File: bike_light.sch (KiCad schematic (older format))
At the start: 0 parts

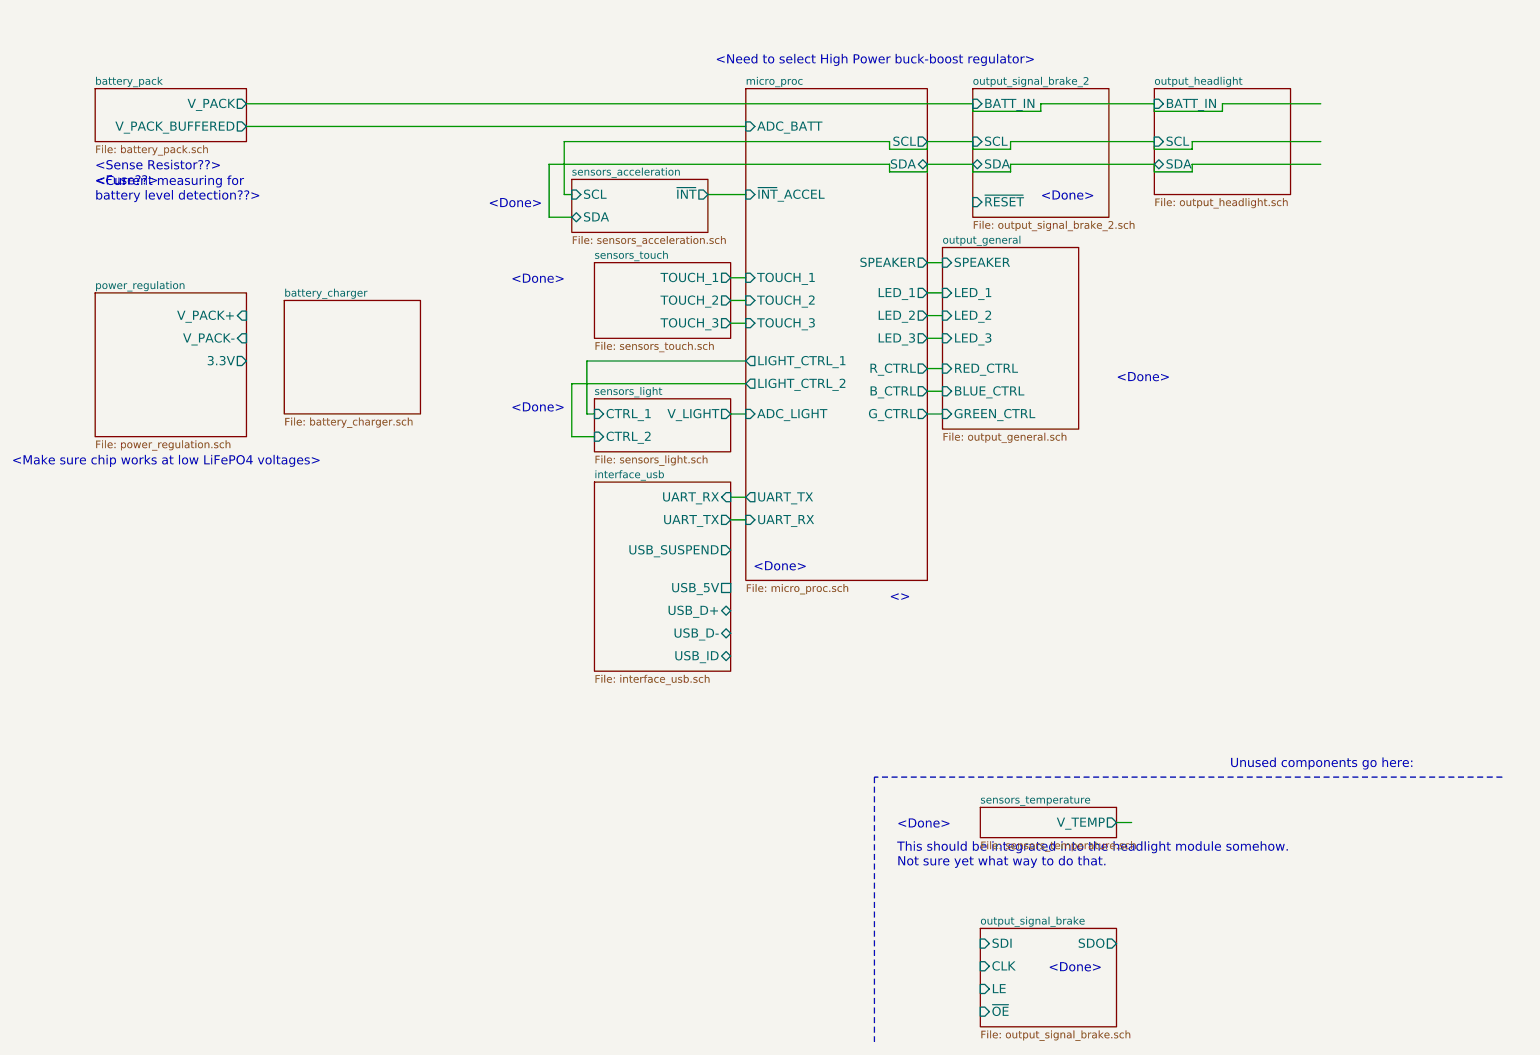
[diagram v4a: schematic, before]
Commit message: general organization, fixed power reg sheet, added jtag
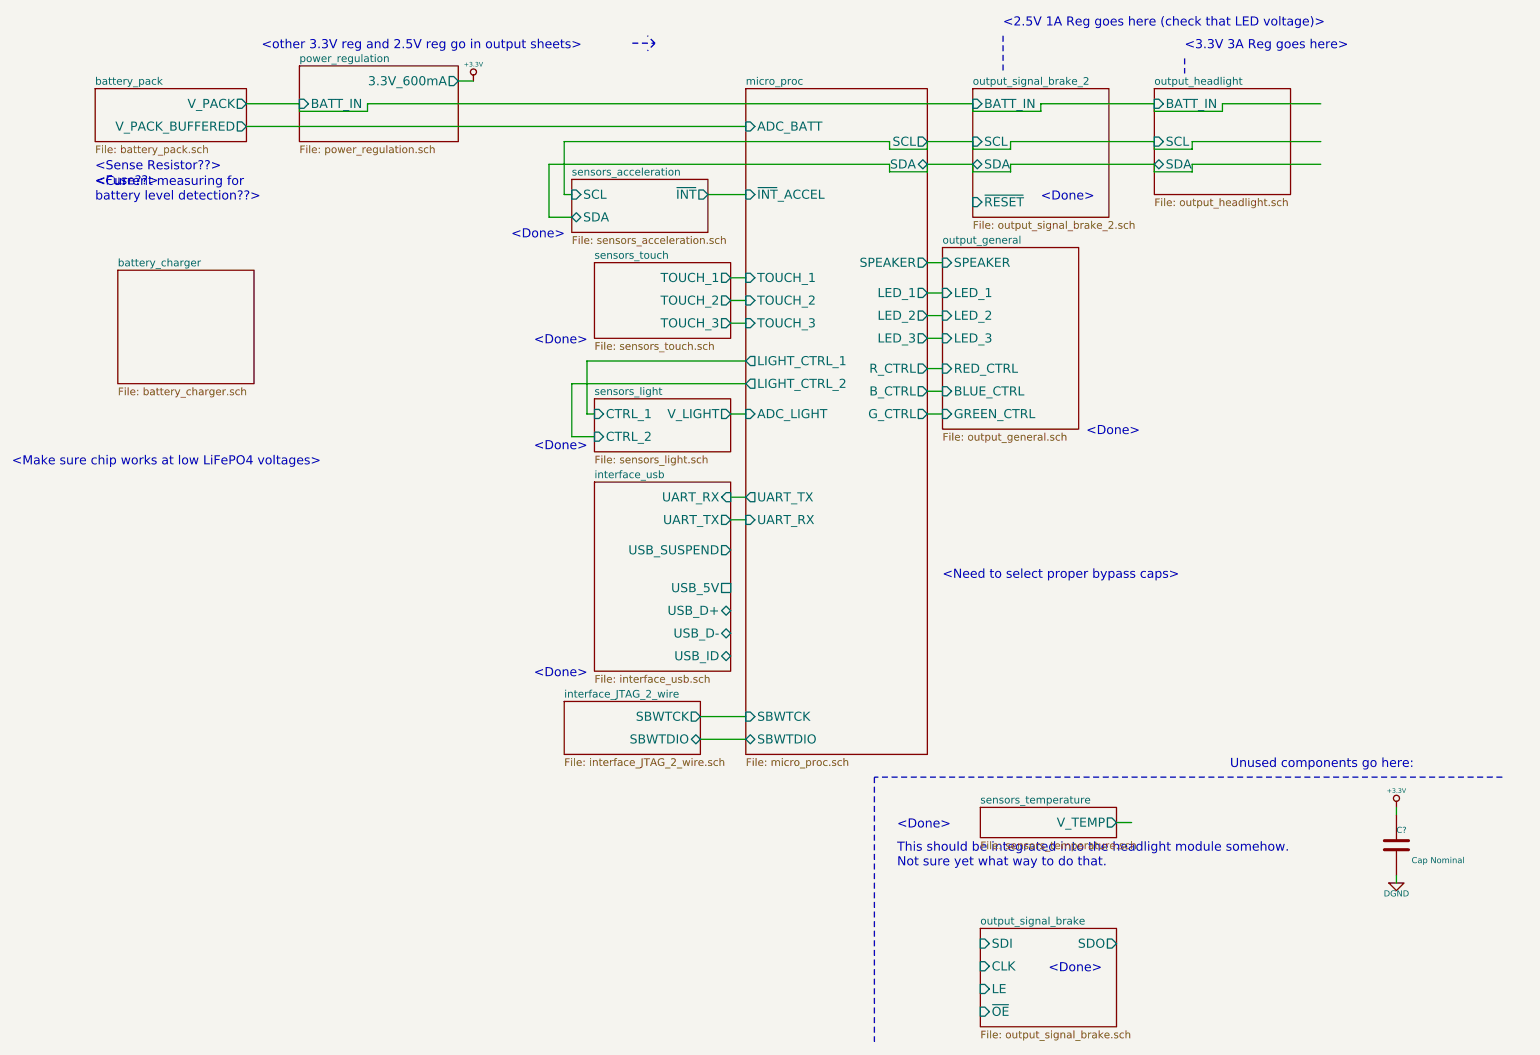
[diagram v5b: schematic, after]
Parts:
- added C?: Cap Nominal, ~, symbol C
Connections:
- net labels added: +3.3V, DGND
- wire segments 61 -> 70
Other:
- note added: "<2.5V 1A Reg goes here (check that LED voltage)>"
- note added: "<3.3V 3A Reg goes here>"
- note added: "<Need to select proper bypass caps>"
- note added: "<other 3.3V reg and 2.5V reg go in output sheets>"
- note removed: "<>"
- note removed: "<Need to select High Power buck-boost regulator>"
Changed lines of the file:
@@
 $Descr USLetter 11000 8500
 encoding utf-8
-Sheet 1 17
+Sheet 1 18
 Title "Bike Light"
 Date "8 dec 2013"
@@
 $EndSheet
 $Sheet
-S 1200 2400 1000 950
-U 5224C4FA
-F0 "power_regulation" 50
-F1 "power_regulation.sch" 50
-F2 "V_PACK+" I R 2200 2550 60
-F3 "V_PACK-" I R 2200 2700 60
-F4 "3.3V" O R 2200 2850 60
-$EndSheet
-$Sheet
-S 5500 1050 1200 3250
+S 5500 1050 1200 4400
 U 5224C543
 F0 "micro_proc" 50
@@
 F19 "UART_RX" I L 5500 3900 60
 F20 "UART_TX" O L 5500 3750 60
+F21 "SBWTCK" I L 5500 5200 60
+F22 "SBWTDIO" B L 5500 5350 60
 $EndSheet
 $Sheet
@@
 F8 "GREEN_CTRL" I L 6800 3200 60
 $EndSheet
-Text Notes 3950 2350 0    60   ~ 0
-<Done>
-Text Notes 3950 3200 0    60   ~ 0
+Text Notes 4100 2750 0    60   ~ 0
+<Done>
+Text Notes 4100 3450 0    60   ~ 0
 <Done>
 Text Notes 6500 5950 0    60   ~ 0
 <Done>
-Text Notes 7950 3000 0    60   ~ 0
+Text Notes 7750 3350 0    60   ~ 0
 <Done>
 Text Notes 7500 6900 0    60   ~ 0
 <Done>
-Text Notes 6450 4450 0    60   ~ 0
-<>
-Text Notes 3800 1850 0    60   ~ 0
+Text Notes 3950 2050 0    60   ~ 0
 <Done>
 Text Notes 1200 1600 0    60   ~ 0
@@
 Text Notes 1200 1800 0    60   ~ 0
 <Current measuring for \nbattery level detection??>
-Text Notes 5550 4250 0    60   ~ 0
+Text Notes 4100 4950 0    60   ~ 0
 <Done>
 Text Notes 650  3550 0    60   ~ 0
 <Make sure chip works at low LiFePO4 voltages>
 $Sheet
-S 2450 2450 900  750
+S 1350 2250 900  750
 U 52929F4D
 F0 "battery_charger" 50
@@
 Text Notes 7450 1800 0    60   ~ 0
 <Done>
-Text Notes 5300 900  0    60   ~ 0
-<Need to select High Power buck-boost regulator>
 Text Notes 6500 6200 0    60   ~ 0
 This should be integrated into the headlight module somehow. \nNot sure yet what way to do that.
@@
 	2200 1300 5500 1300
 Wire Wire Line
-	2200 1150 7000 1150
-Wire Wire Line
 	6450 1400 6450 1450
 Wire Wire Line
@@
 Wire Wire Line
 	5400 3900 5500 3900
+$Comp
+L +3.3V #PWR?
+U 1 1 52A50B64
+P 3700 1000
+F 0 "#PWR?" H 3700 960 30  0001 C CNN
+F 1 "+3.3V" H 3700 1110 30  0000 C CNN
+F 2 "" H 3700 1000 60  0000 C CNN
+F 3 "" H 3700 1000 60  0000 C CNN
+	1    3700 1000
+	1    0    0    -1
+$EndComp
+Wire Wire Line
+	3600 1000 3700 1000
+$Sheet
+S 2550 900  1050 500
+U 5224C4FA
+F0 "power_regulation" 50
+F1 "power_regulation.sch" 50
+F2 "3.3V_600mA" O R 3600 1000 60
+F3 "BATT_IN" I L 2550 1150 60
+$EndSheet
+Wire Wire Line
+	2200 1150 2550 1150
+Wire Wire Line
+	2550 1150 2550 1200
+Wire Wire Line
+	2550 1200 3000 1200
+Wire Wire Line
+	3000 1200 3000 1150
+Wire Wire Line
+	3000 1150 7000 1150
+Text Notes 2300 800  0    60   ~ 0
+<other 3.3V reg and 2.5V reg go in output sheets>
+Text Notes 7200 650  0    60   ~ 0
+<2.5V 1A Reg goes here (check that LED voltage)>
+Wire Notes Line
+	7200 700  7200 950
+Text Notes 8400 800  0    60   ~ 0
+<3.3V 3A Reg goes here>
+Wire Notes Line
+	8400 850  8400 950
+Wire Notes Line
+	4750 750  4900 750
+Wire Notes Line
+	4900 750  4850 800
+Wire Notes Line
+	4900 750  4850 700
+Text Notes 6800 4300 0    60   ~ 0
+<Need to select proper bypass caps>
+$Sheet
+S 4300 5100 900  350
+U 52A6745A
+F0 "interface_JTAG_2_wire" 50
+F1 "interface_JTAG_2_wire.sch" 50
+F2 "SBWTCK" O R 5200 5200 60
+F3 "SBWTDIO" B R 5200 5350 60
+$EndSheet
+$Comp
+L C C?
+U 1 1 52A6923B
+P 9800 6050
+F 0 "C?" H 9800 6150 40  0000 L CNN
+F 1 "Cap Nominal" H 9900 5950 40  0000 L CNN
+F 2 "~" H 9838 5900 30  0000 C CNN
+F 3 "~" H 9800 6050 60  0000 C CNN
+	1    9800 6050
+	1    0    0    -1
+$EndComp
+$Comp
+L +3.3V #PWR?
+U 1 1 52A69241
+P 9800 5800
+F 0 "#PWR?" H 9800 5760 30  0001 C CNN
+F 1 "+3.3V" H 9800 5910 30  0000 C CNN
+F 2 "" H 9800 5800 60  0000 C CNN
+F 3 "" H 9800 5800 60  0000 C CNN
+	1    9800 5800
+	1    0    0    -1
+$EndComp
+$Comp
+L DGND #PWR?
+U 1 1 52A69247
+P 9800 6300
+F 0 "#PWR?" H 9800 6300 40  0001 C CNN
+F 1 "DGND" H 9800 6230 40  0000 C CNN
+F 2 "" H 9800 6300 60  0000 C CNN
+F 3 "" H 9800 6300 60  0000 C CNN
+	1    9800 6300
+	1    0    0    -1
+$EndComp
+Wire Wire Line
+	9800 5800 9800 5850
+Wire Wire Line
+	9800 6250 9800 6300
+Wire Wire Line
+	5200 5200 5500 5200
+Wire Wire Line
+	5200 5350 5500 5350
 $EndSCHEMATC
